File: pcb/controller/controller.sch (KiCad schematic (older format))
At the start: 72 parts, among them J0 JST-HX_01x03, J1 Conn_01x24, J2 Conn_01x24, J3 Conn_01x05, J4 Conn_01x01, J5 Barrel_Jack, SW1 Button, SW2 Button, SW4 Button, U1 Teensy4.1

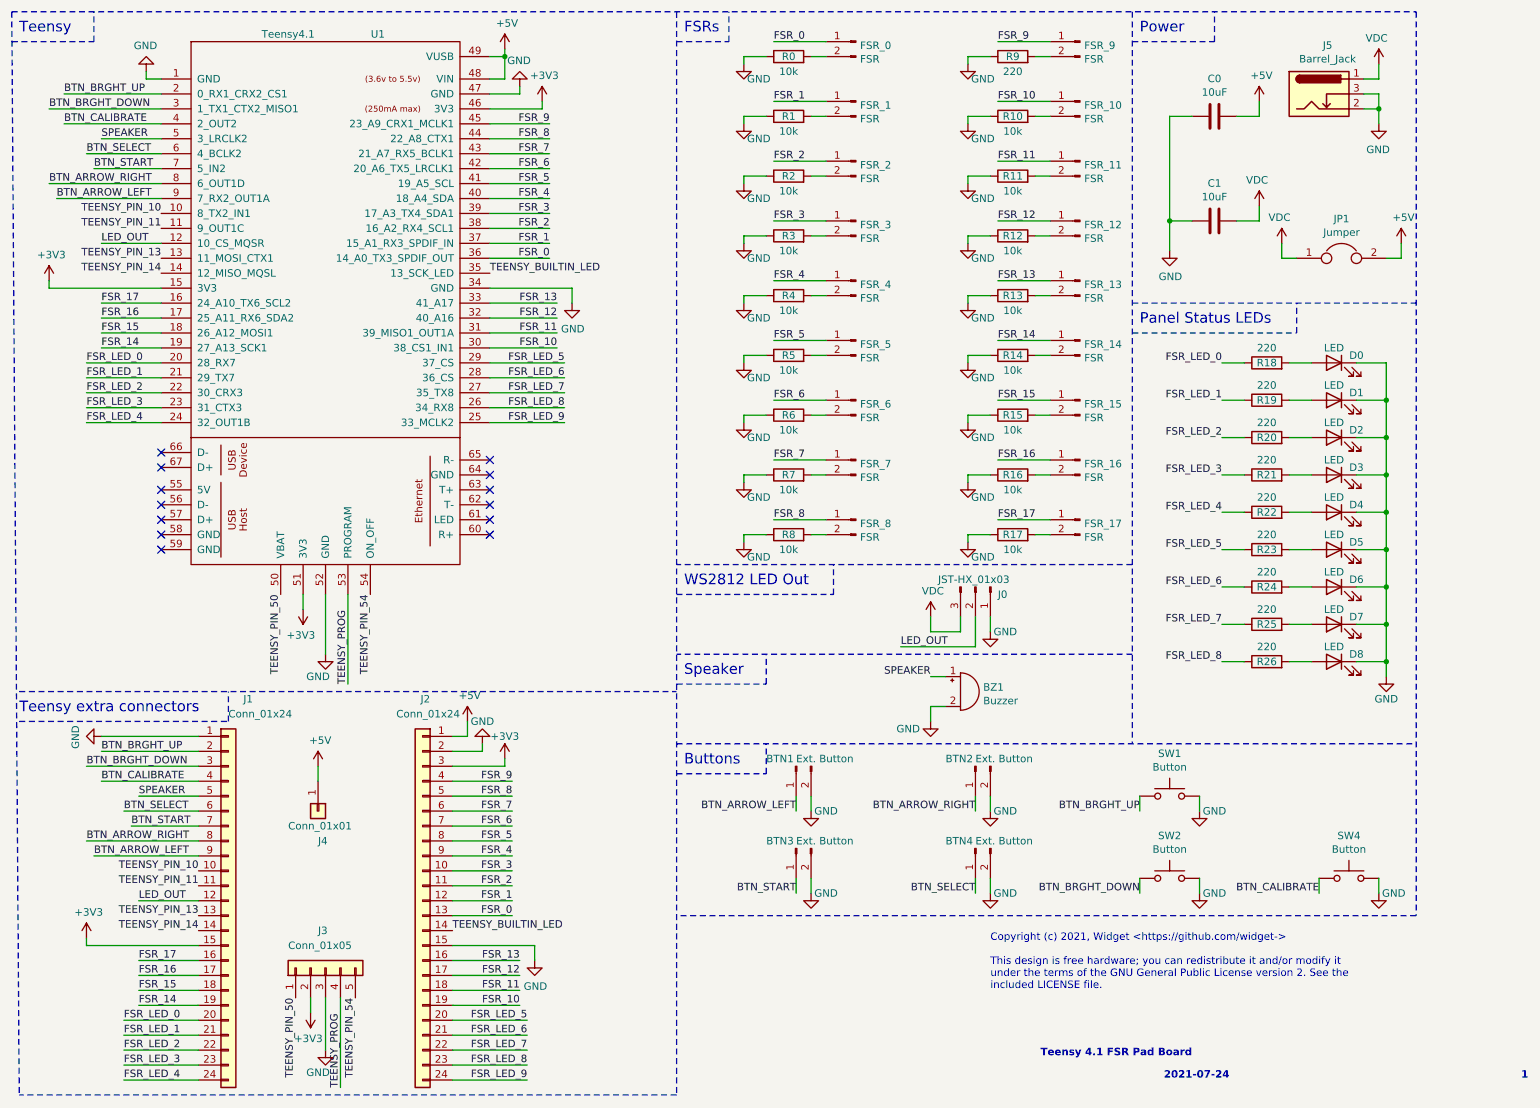
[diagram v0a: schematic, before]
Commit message: Finalize v0.1 of breakout board to start v0.2
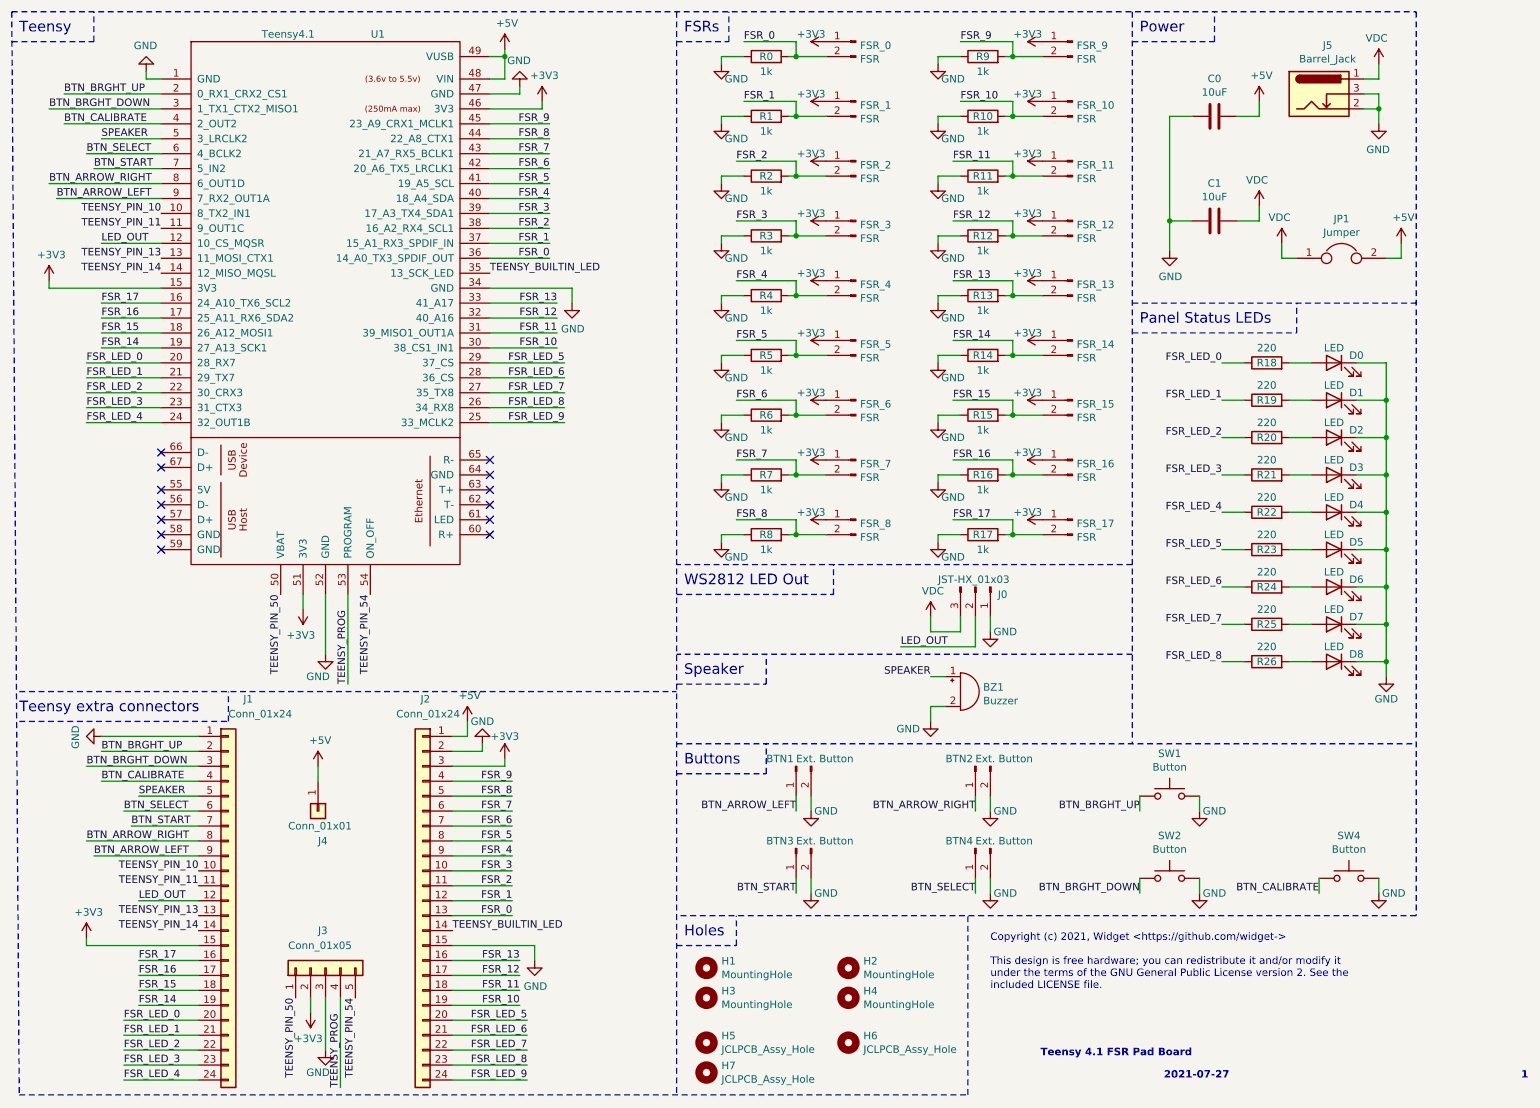
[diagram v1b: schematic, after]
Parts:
- added H1, H2, H3, H4: MountingHole, MountingHole:MountingHole_3.2mm_M3, symbol Mechanical:MountingHole
- added H5, H6, H7: JCLPCB_Assy_Hole, widgetpad_parts:JCLPCB_Assembly_Hole, symbol Mechanical:MountingHole
- R0, R1, R10, R11, R12, R13, R14, R15, R16, R17, R2, R3, R4, R5, R6, R7, R8: value 10k -> 1k
- R9: value 220 -> 1k
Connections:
- net +3V3: now also FSR_0.1 (Pin_1), FSR_1.1 (Pin_1), FSR_10.1 (Pin_1), FSR_11.1 (Pin_1), FSR_12.1 (Pin_1), FSR_13.1 (Pin_1), FSR_14.1 (Pin_1), FSR_15.1 (Pin_1), FSR_16.1 (Pin_1), FSR_17.1 (Pin_1), FSR_2.1 (Pin_1), FSR_3.1 (Pin_1), FSR_4.1 (Pin_1), FSR_5.1 (Pin_1), FSR_6.1 (Pin_1), FSR_7.1 (Pin_1), FSR_8.1 (Pin_1), FSR_9.1 (Pin_1)
- net FSR_0: now also FSR_0.2 (Pin_2), R0.2; no longer FSR_0.1 (Pin_1)
- net FSR_1: now also FSR_1.2 (Pin_2), R1.2; no longer FSR_1.1 (Pin_1)
- net FSR_10: now also FSR_10.2 (Pin_2), R10.2; no longer FSR_10.1 (Pin_1)
- net FSR_11: now also FSR_11.2 (Pin_2), R11.2; no longer FSR_11.1 (Pin_1)
- net FSR_12: now also FSR_12.2 (Pin_2), R12.2; no longer FSR_12.1 (Pin_1)
- net FSR_13: now also FSR_13.2 (Pin_2), R13.2; no longer FSR_13.1 (Pin_1)
- net FSR_14: now also FSR_14.2 (Pin_2), R14.2; no longer FSR_14.1 (Pin_1)
- net FSR_15: now also FSR_15.2 (Pin_2), R15.2; no longer FSR_15.1 (Pin_1)
- net FSR_16: now also FSR_16.2 (Pin_2), R16.2; no longer FSR_16.1 (Pin_1)
- net FSR_17: now also FSR_17.2 (Pin_2), R17.2; no longer FSR_17.1 (Pin_1)
- net FSR_2: now also FSR_2.2 (Pin_2), R2.2; no longer FSR_2.1 (Pin_1)
- net FSR_3: now also FSR_3.2 (Pin_2), R3.2; no longer FSR_3.1 (Pin_1)
- net FSR_4: now also FSR_4.2 (Pin_2), R4.2; no longer FSR_4.1 (Pin_1)
- net FSR_5: now also FSR_5.2 (Pin_2), R5.2; no longer FSR_5.1 (Pin_1)
- net FSR_6: now also FSR_6.2 (Pin_2), R6.2; no longer FSR_6.1 (Pin_1)
- net FSR_7: now also FSR_7.2 (Pin_2), R7.2; no longer FSR_7.1 (Pin_1)
- net FSR_8: now also FSR_8.2 (Pin_2), R8.2; no longer FSR_8.1 (Pin_1)
- net FSR_9: now also FSR_9.2 (Pin_2), R9.2; no longer FSR_9.1 (Pin_1)
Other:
- note added: "2021-07-27"
- note added: "Holes"
- note removed: "2021-07-24"
- moved on the sheet: R0, R1, R2, R3, R4, R5, R6, R7, R8
